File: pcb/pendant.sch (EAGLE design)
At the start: 76 parts, among them CON1 USB_MICROSMT+THRUHULE, Q2 16MHz, SW2 BUTTON_2, T1 SSM3J328R,LF, T2 SSM3J328R,LF, U2 MK20D--VFM5, U3 74LVC1G17DCK, U4 74LVC1G17DCK

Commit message: Update reference designators
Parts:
- removed C13: 100nF, adafruit:C-USC0402
- removed U$6: MMA8653FC, teensy_adapter:MMA8653FC
- added C4: 100nF, adafruit:C-USC0402
- added U1: MK20D--VFM5, blinkinlabs:MK20D--VFM5
- U2: value MK20D--VFM5 -> MMA8653FC; device blinkinlabs:MK20D--VFM5 -> teensy_adapter:MMA8653FC
- renumbered C11 to C6, C12 to C10, C14 to C8, C15 to C7, C17 to C9, U$1 to CON2, U$2 to SW1, U4 to U5
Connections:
- net +5V: now also U1.VREGIN; no longer U2.VREGIN
- net 3.3V: now also C4.1, U1.VBAT, U1.VDD, U1.VDDA, U1.VOUT33, U2.VDDIO; no longer C13.1, U$6.VDD, U$6.VDDIO, U2.VBAT, U2.VDDA, U2.VOUT33
- net ACC_INT1: now also U1.PTC3, U2.INT1; no longer U$6.INT1, U2.PTC3
- net GND: now also C4.2, U1.VSS, U1.VSSA, U2.GND; no longer C13.2, U$6.GND, U2.VSS, U2.VSSA
- net I2C0_SCL: now also U1.PTB0, U2.SCL; no longer U$6.SCL, U2.PTB0
- net I2C0_SDA: now also U1.PTB1, U2.SDA; no longer U$6.SDA, U2.PTB1
- net LED_CLOCK: now also U1.PTC5; no longer U2.PTC5
- net LED_DATA: now also U1.PTC6; no longer U2.PTC6
- net LED_OE: now also U1.PTA4; no longer U2.PTA4
- net LED_S0: now also U1.PTD4; no longer U2.PTD4
- net LED_S1: now also U1.PTD5; no longer U2.PTD5
- net LED_STROBE: now also U1.PTD6; no longer U2.PTD6
- net N$13: now also U1.PTA19; no longer U2.PTA19
- net N$15: now also U1.USB0_DM; no longer U2.USB0_DM
- net N$17: now also U1.USB0_DP; no longer U2.USB0_DP
- net N$4: now also U2.BYP; no longer U$6.BYP
- net N$8: now also U1.PTA18; no longer U2.PTA18
- net RESET: now also U1.RESET_B; no longer U2.RESET_B
- net RX: now also U1.PTA1; no longer U2.PTA1
- net TCLK: now also U1.PTA0; no longer U2.PTA0
- net TMS: now also U1.PTA3; no longer U2.PTA3
- net TX: now also U1.PTA2; no longer U2.PTA2
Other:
- moved on the sheet: C5

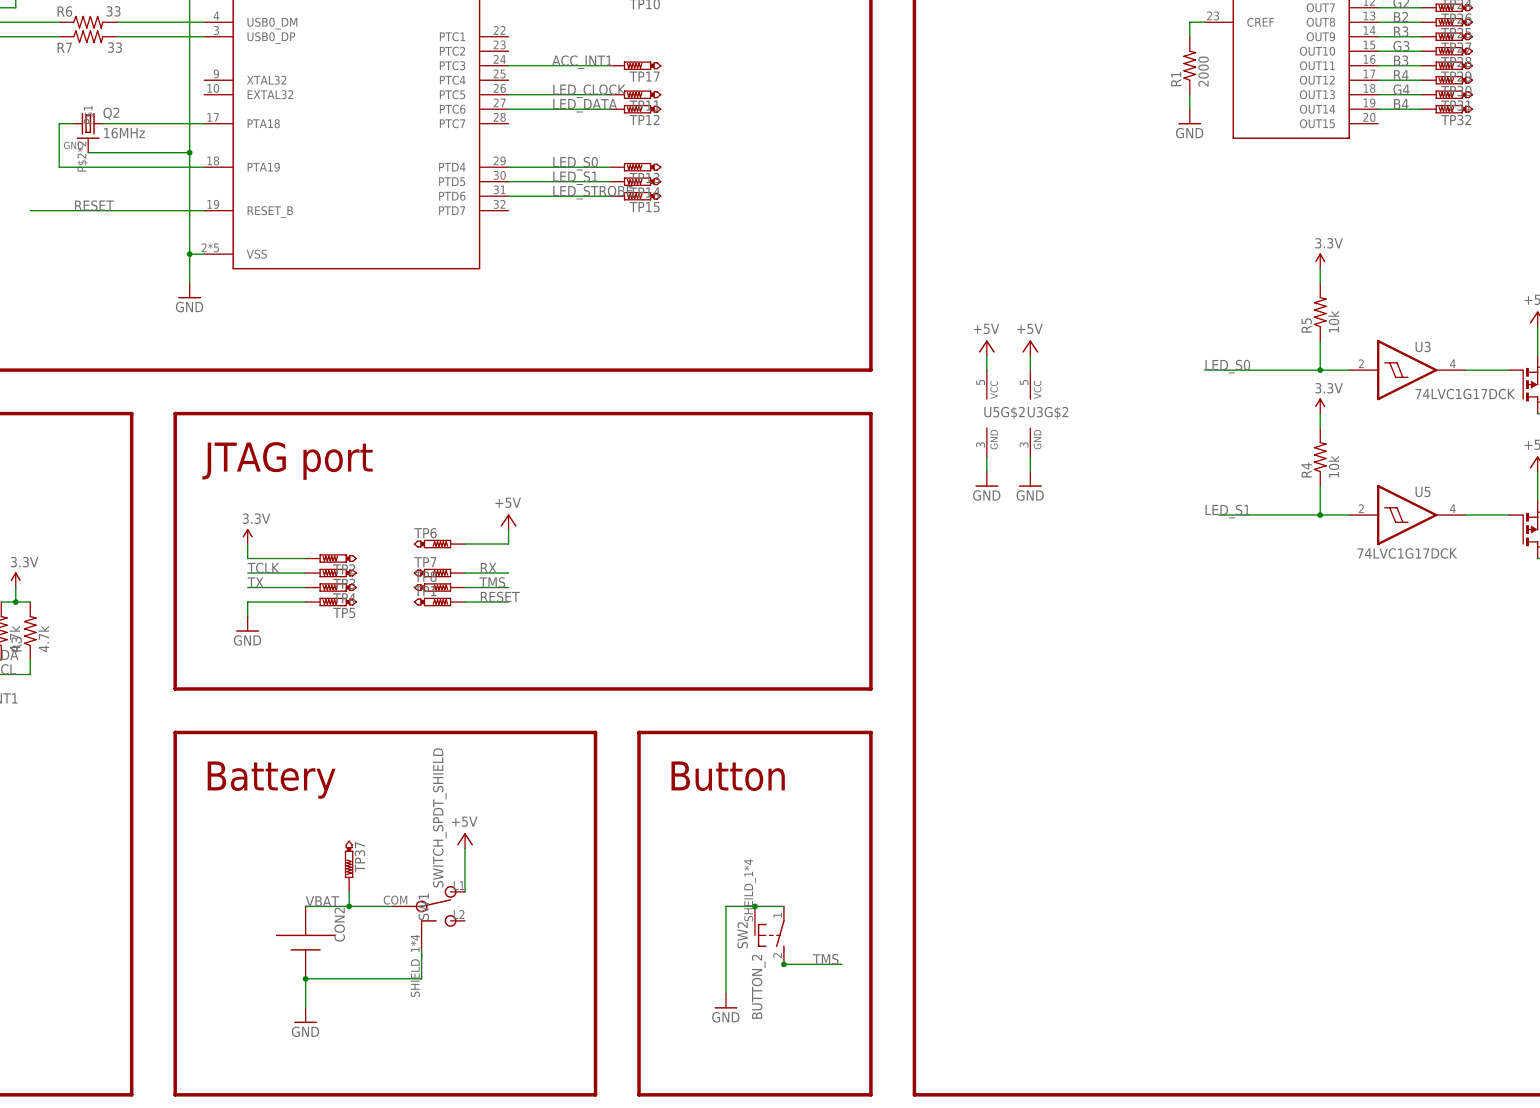
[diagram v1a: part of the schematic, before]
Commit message: Update reference designators on the BOM
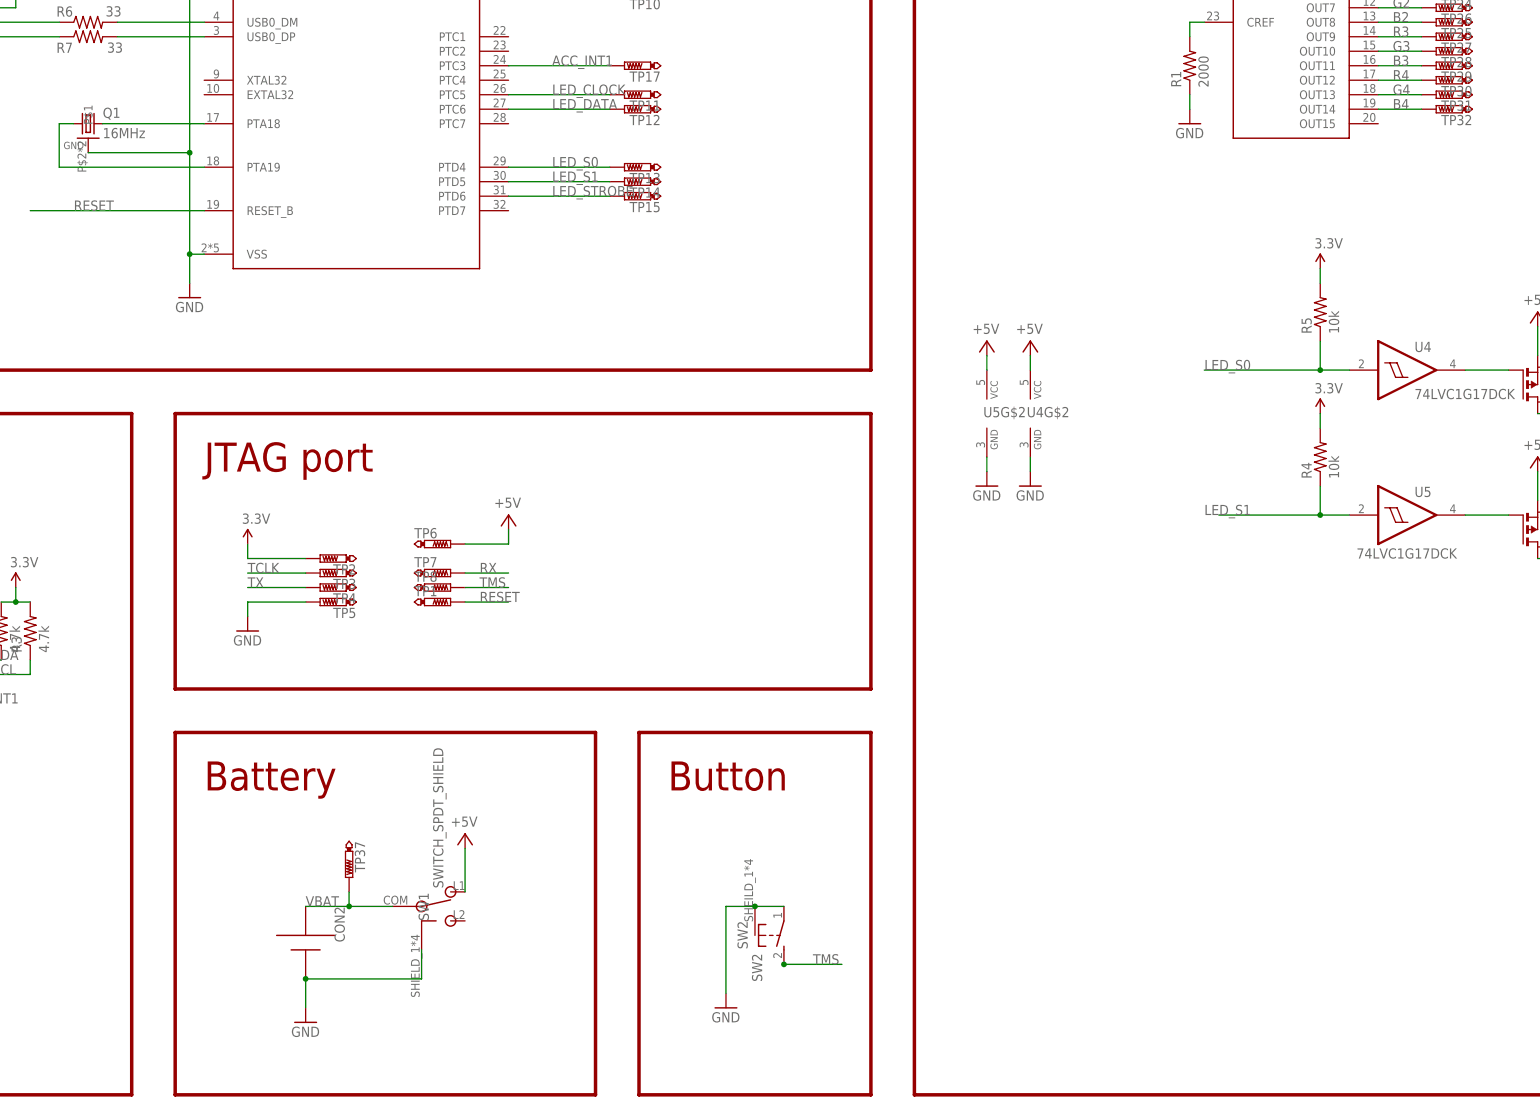
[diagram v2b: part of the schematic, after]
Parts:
- removed U$5: ICN2026DF, teensy_adapter:ICN2026DF
- added U4: 74LVC1G17DCK, 74xx-little-us:74LVC1G17DCK
- SW2: value BUTTON_2 -> SW2
- U3: value 74LVC1G17DCK -> ICN2026DF; device 74xx-little-us:74LVC1G17DCK -> teensy_adapter:ICN2026DF
- renumbered Q2 to Q1
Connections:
- net +5V: now also U4G$2.VCC; no longer U3G$2.VCC
- net 3.3V: now also U3.VCC; no longer U$5.VCC
- net B0: now also U3.OUT2; no longer U$5.OUT2
- net B1: now also U3.OUT5; no longer U$5.OUT5
- net B2: now also U3.OUT8; no longer U$5.OUT8
- net B3: now also U3.OUT11; no longer U$5.OUT11
- net B4: now also U3.OUT14; no longer U$5.OUT14
- net G0: now also U3.OUT1; no longer U$5.OUT1
- net G1: now also U3.OUT4; no longer U$5.OUT4
- net G2: now also U3.OUT7; no longer U$5.OUT7
- net G3: now also U3.OUT10; no longer U$5.OUT10
- net G4: now also U3.OUT13; no longer U$5.OUT13
- net GND: now also U3.GND, U4G$2.GND; no longer U$5.GND, U3G$2.GND
- net LED_CLOCK: now also U3.CLK; no longer U$5.CLK
- net LED_DATA: now also U3.DIN; no longer U$5.DIN
- net LED_OE: now also U3.OE; no longer U$5.OE
- net LED_S0: now also U4G$1.I; no longer U3G$1.I
- net LED_STROBE: now also U3.LATCH; no longer U$5.LATCH
- net N$18: now also U3.CREF; no longer U$5.CREF
- net N$6: now also U4G$1.O; no longer U3G$1.O
- net R0: now also U3.OUT0; no longer U$5.OUT0
- net R1: now also U3.OUT3; no longer U$5.OUT3
- net R2: now also U3.OUT6; no longer U$5.OUT6
- net R3: now also U3.OUT9; no longer U$5.OUT9
- net R4: now also U3.OUT12; no longer U$5.OUT12
